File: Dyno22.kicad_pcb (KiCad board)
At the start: 2 copper layers, 53 parts, among them J1 Pwr Input, J2 Display, J3 Pwr Output, J4 BPM & Sensors, J7 UART, SW1 SW_DPST_x2, U1 TS2937CW50, U2 LM324, U3 Demux

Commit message: Through hole adjustments and some routing changes
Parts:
- TP2, TP3: footprint TestPoint:TestPoint_Loop_D2.60mm_Drill1.6mm_Beaded -> TestPoint:TestPoint_Plated_Hole_D2.0mm
- TP4, TP5: footprint TestPoint:TestPoint_Loop_D2.60mm_Drill1.4mm_Beaded -> TestPoint:TestPoint_Plated_Hole_D2.0mm
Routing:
- net /KILL_SW: track 82.9 -> 82.1 mm

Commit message: move around the rot encoder
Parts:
- moved R3 19.0 mm to (171.7, 110.6), turned to -90 degrees
- moved S3 16.6 mm to (151.7, 106.9)
- moved R4 16.1 mm to (115.9, 114.3)
- moved R5 15.9 mm to (115.9, 110.1)
- moved Encoder1 15.4 mm to (124.8, 111.7)
- moved S2 12.3 mm to (93.4, 106.9)
- moved R1 8.86 mm to (116.0, 118.7), turned to 0 degrees
- moved S1 4.32 mm to (70.4, 106.9)
- moved R2 3.21 mm to (90.6, 110.9)
- moved RV1 2.76 mm to (205.7, 123.2)
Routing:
- net /ROT_EN_SW: track 49.3 -> 94.8 mm
- net /LED_SELECT: track 79.9 -> 113.7 mm, vias 0 -> 1
- net Earth: track 44.1 -> 59.7 mm
- net /ROT_EN_B: track 88.8 -> 103.9 mm
- net /ROT_EN_A: track 83.0 -> 97.9 mm
- net Net-(S3-L1_Y): track 15.8 -> 27.8 mm
- net /BTN_SELECT: track 79.6 -> 89.4 mm
- net /BTN_BRAKE: track 19.8 -> 29.5 mm
- net /BTN_BACK: track 108.4 -> 112.4 mm
- net Net-(S2-L1_Y): track 11.0 -> 14.8 mm
- net /BPM_CTRL_IN: track 69.8 -> 73.2 mm
- net Net-(S1-L2_G): track 11.6 -> 12.6 mm
- net /LED_BACK: track 111.2 -> 111.5 mm, vias 0 -> 1

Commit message: updated encoder
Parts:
- C2: footprint Capacitor_Tantalum_SMD:CP_EIA-6032-20_AVX-F -> CAP_293D-C_VSS:CAP_293D-C_VSS
- Encoder: renamed from Encoder1; footprint Rotary_Encoder:RotaryEncoder_Alps_EC12E-Switch_Vertical_H20mm_CircularMountingHoles -> PEC11R_4215F_S0024:TO_215F-S0024
- TP1: footprint TestPoint:TestPoint_Loop_D2.60mm_Drill1.4mm_Beaded -> TestPoint:TestPoint_Plated_Hole_D2.0mm
- moved R3 24.8 mm to (148.1, 118.3), turned to 90 degrees
- moved Encoder 14.3 mm to (139.1, 112.0), turned to -90 degrees
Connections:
- Encoder pad B: /ROT_EN_B -> Earth
- Encoder pad C: Earth -> /ROT_EN_B
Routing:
- net /ROT_EN_SW: track 94.8 -> 68.5 mm

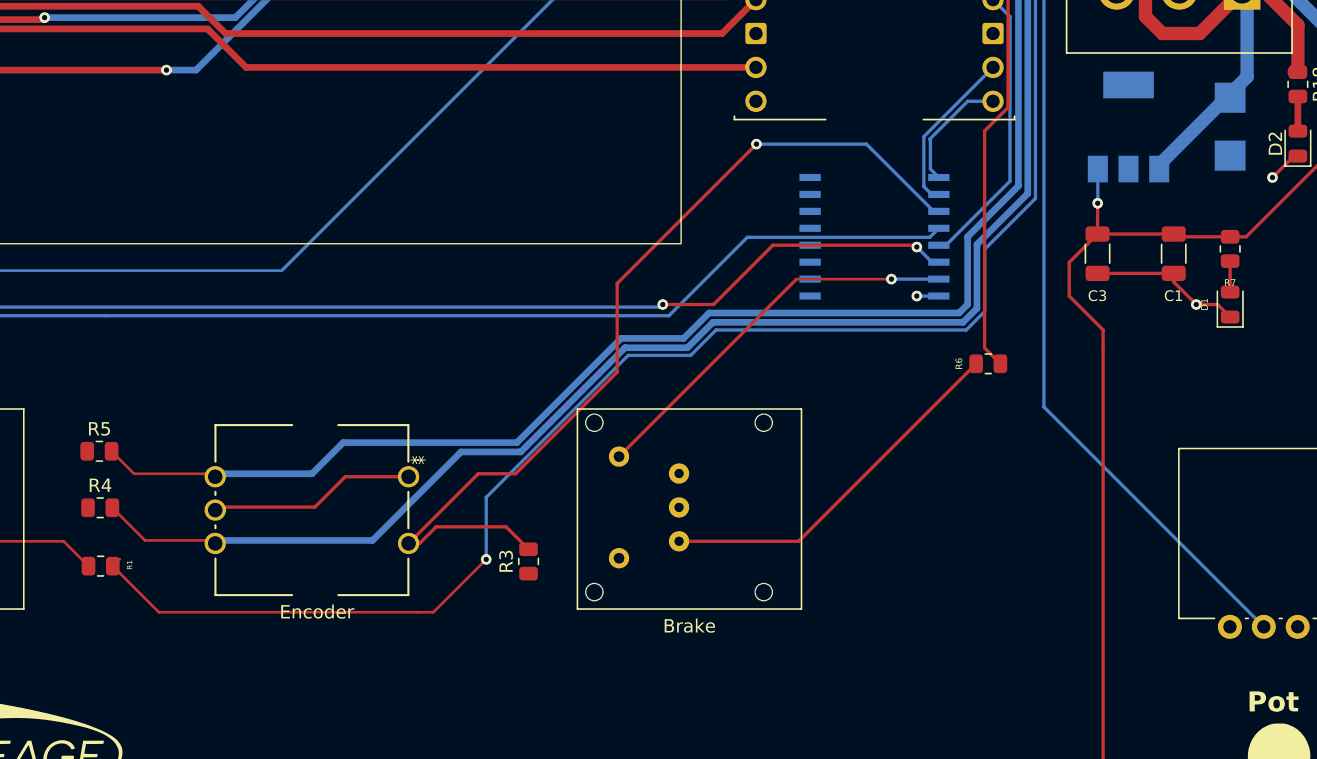
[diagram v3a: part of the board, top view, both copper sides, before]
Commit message: added encoder filter circuit
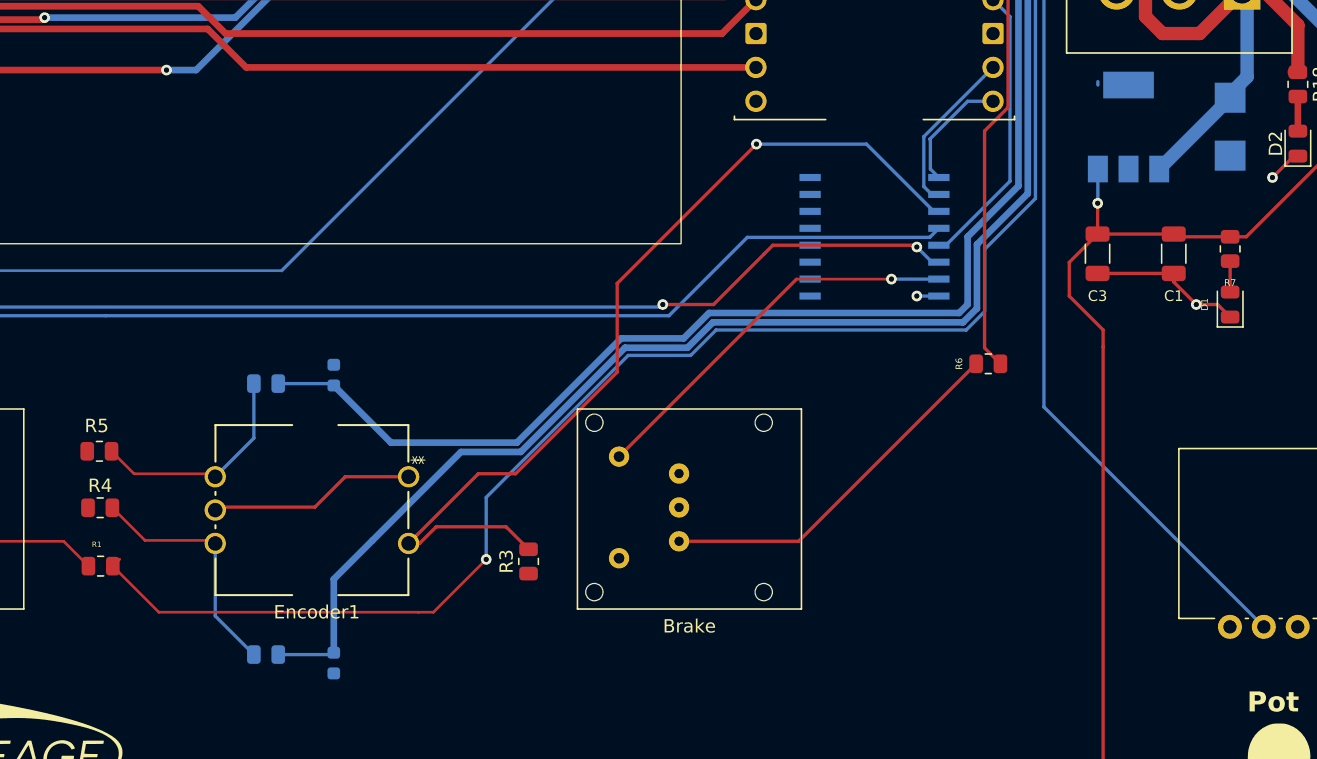
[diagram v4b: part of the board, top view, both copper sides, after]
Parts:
- added C6: 0.01uF, Capacitor_SMD:C_0603_1608Metric, B.Cu at (133.4, 104.4)
- added C7: 0.01uF, Capacitor_SMD:C_0603_1608Metric, B.Cu at (133.4, 125.9)
- added R19: 10kΩ, Resistor_SMD:R_0805_2012Metric, B.Cu at (128.4, 105.0)
- added R20: 10kΩ, Resistor_SMD:R_0805_2012Metric, B.Cu at (128.4, 125.3)
- renumbered Encoder to Encoder1
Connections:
- Encoder1 pad A: /ROT_EN_A -> Net-(Encoder1-PadA)
- Encoder1 pad C: /ROT_EN_B -> Net-(Encoder1-PadC)
- R4 pad 2: /ROT_EN_B -> Net-(Encoder1-PadC)
- R5 pad 2: /ROT_EN_A -> Net-(Encoder1-PadA)
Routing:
- net Net-(Encoder1-PadC): track 0.00 -> 18.5 mm
- net Net-(Encoder1-PadA): track 0.00 -> 16.9 mm
- net /ROT_EN_A: track 97.9 -> 85.6 mm
- net /ROT_EN_B: track 103.9 -> 97.3 mm

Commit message: v2
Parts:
- Back: renamed from S1; footprint LP11EE1NCSYG:LP11EE1NCSYG -> KP0115ANBKG03RGBP3SJB:KP0115ANBKG03RGBP3SJB
- R4, R5: value 10kΩ -> 1kΩ
- Select: renamed from S2; footprint LP11EE1NCSYG:LP11EE1NCSYG -> KP0115ANBKG03RGBP3SJB:KP0115ANBKG03RGBP3SJB
- U2: moved to F.Cu
- moved U2 15.1 mm to (188.7, 67.3)
- moved R15 12.6 mm to (190.0, 64.3), turned to 180 degrees
- moved Back 11.9 mm to (73.7, 118.3), turned to 90 degrees
- moved Select 11.9 mm to (96.6, 118.3), turned to 90 degrees
- moved R2 8.49 mm to (89.6, 102.5), turned to 0 degrees
- moved H1 4.00 mm to (212.5, 132.5)
- moved R12 2.93 mm to (195.0, 64.3), turned to 0 degrees
- renumbered Encoder1 to Encoder, SW1 to ON/OFF
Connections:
- Back pad 2: /BTN_BACK -> +3.3V
- R1 pad 1: Net-(S2-L1_Y) -> Net-(S2-K_B)
- R2 pad 1: Net-(S1-L2_G) -> Net-(S1-K_R)
- Select pad 2: /BTN_SELECT -> +3.3V
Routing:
- net Net-(S2-K_B): track 0.00 -> 18.6 mm
- net Net-(S1-K_R): track 0.00 -> 16.5 mm
- net /BPM_CTRL: track 22.5 -> 37.8 mm
- net Net-(S2-L1_Y): track 14.8 -> 0.00 mm
- net Net-(S1-L2_G): track 12.6 -> 0.00 mm
- net Earth: track 59.5 -> 68.7 mm, vias 2 -> 3
- net /LED_BACK: track 111.5 -> 108.5 mm
- net Net-(U2-+): track 16.0 -> 15.0 mm, vias 0 -> 1
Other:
- board outline added: 160.7 x 109.9 mm
- board text added: "Dyno Control v2"
- board text removed: "Dyno Control"

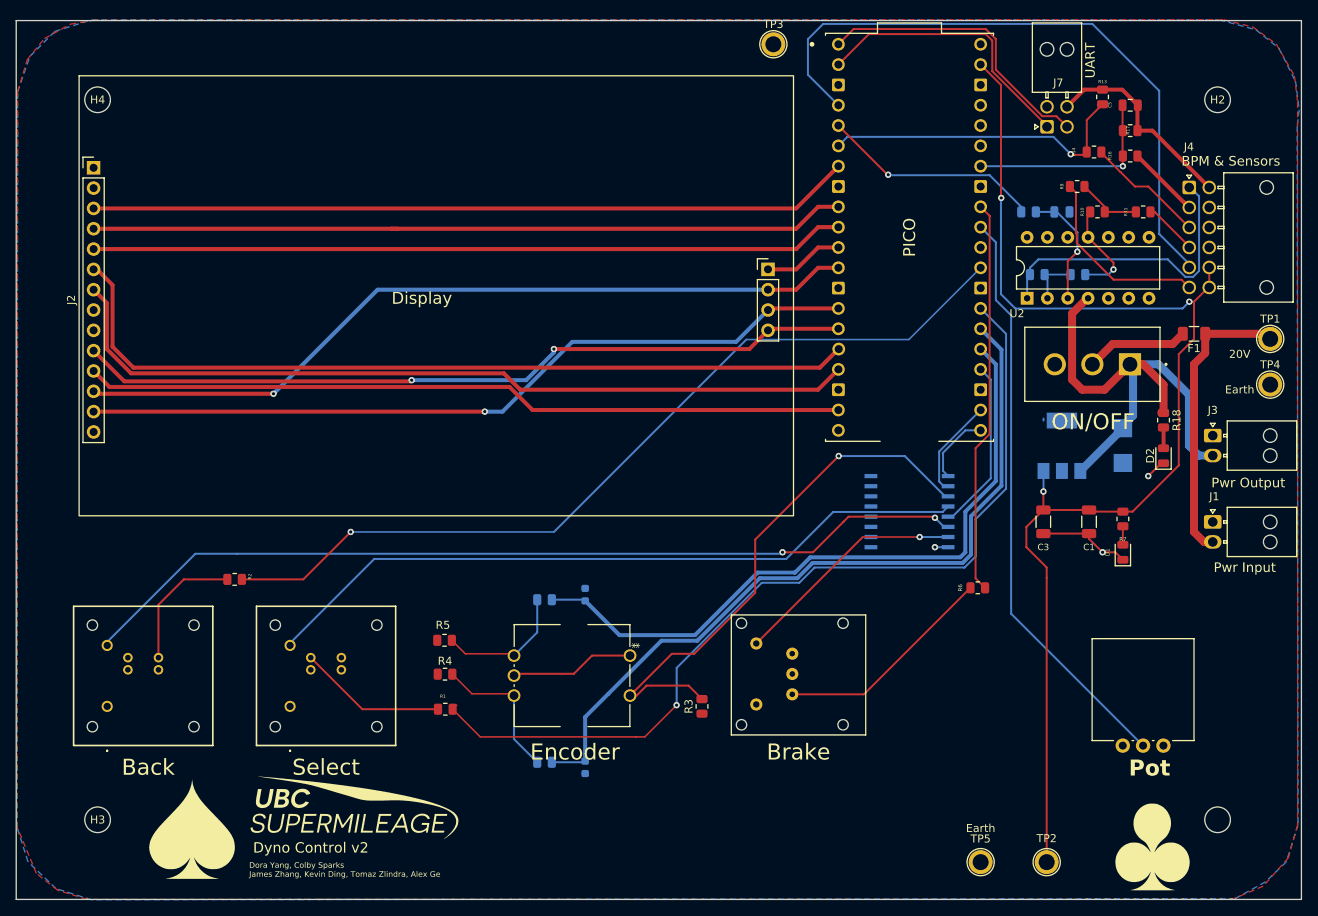
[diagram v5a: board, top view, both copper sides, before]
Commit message: eliminated demux dead zone
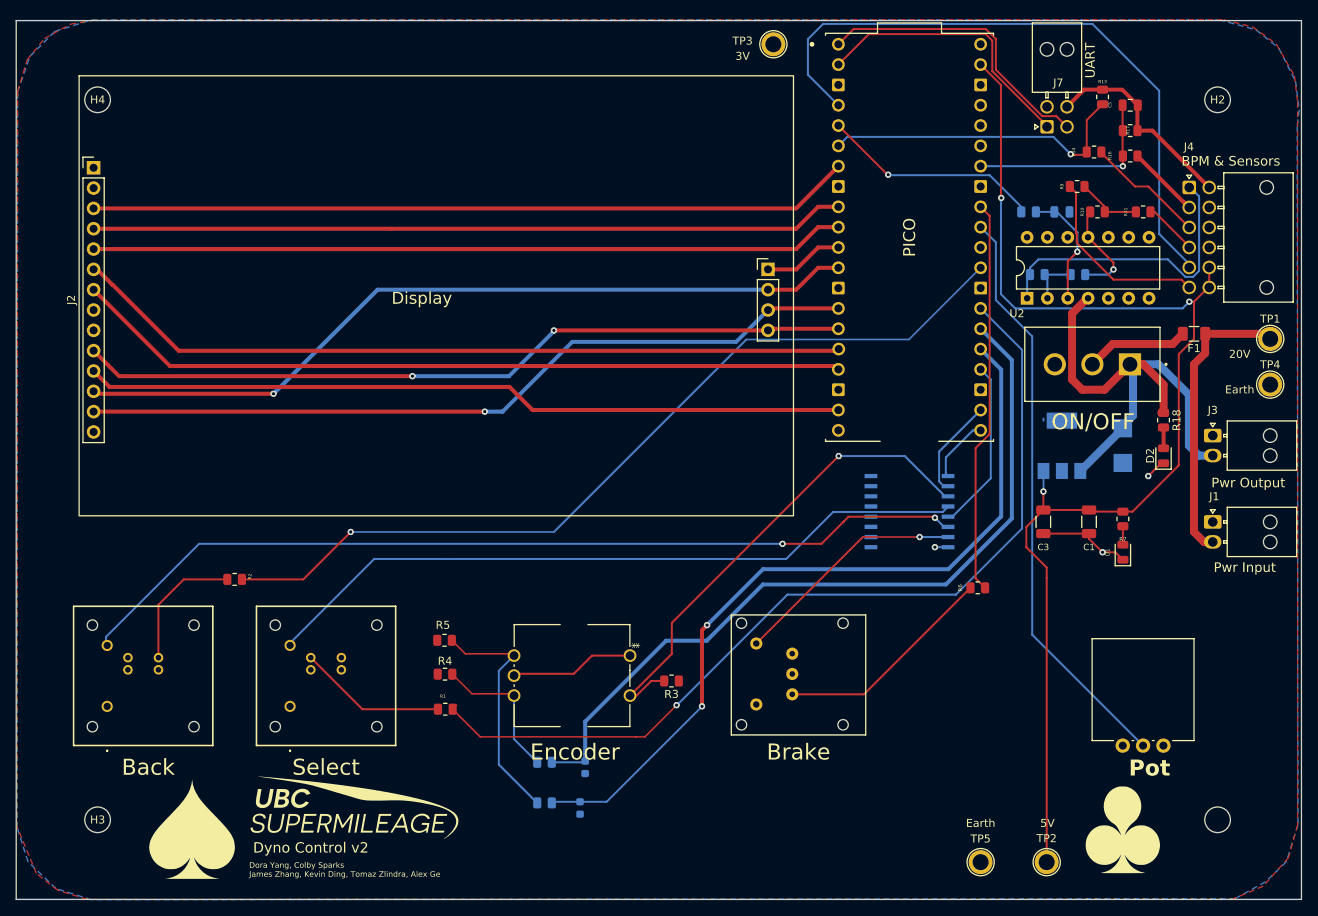
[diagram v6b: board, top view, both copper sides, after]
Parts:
- moved C6 26.7 mm to (132.8, 131.0), turned to 90 degrees
- moved R19 25.4 mm to (128.4, 130.4)
- moved R3 4.96 mm to (144.2, 115.2), turned to 180 degrees
- moved GW 4.29 mm to (200.8, 133.7)
- renumbered G*** to GW
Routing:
- net Net-(Encoder1-PadA): track 16.9 -> 29.9 mm
- net /ROT_EN_A: track 85.6 -> 98.6 mm, vias 0 -> 2
- net /ROT_EN_SW: track 68.5 -> 61.7 mm
- net /MOSI_0: track 103.7 -> 97.4 mm
- net /SCLK_0: track 102.7 -> 97.2 mm
- net /ROT_EN_B: track 97.3 -> 98.4 mm
- net /DEMUX_S1: track 9.11 -> 8.24 mm
- net /LCD_RST: track 95.1 -> 94.2 mm
- net /SCLK_1: track 97.7 -> 96.9 mm
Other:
- board text added: "3V"
- board text added: "5V"
